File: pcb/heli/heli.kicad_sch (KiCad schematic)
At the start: 33 parts, among them J1 Batterie, J2 Debug, J4 Servo, J5 Servo, Q1 IRLZ44N, SW1 SW_MEC_5E, U1 AZ1117-3.3, U2 MPU-6050, U3 STM32F103CBTx, Y1 8MHz

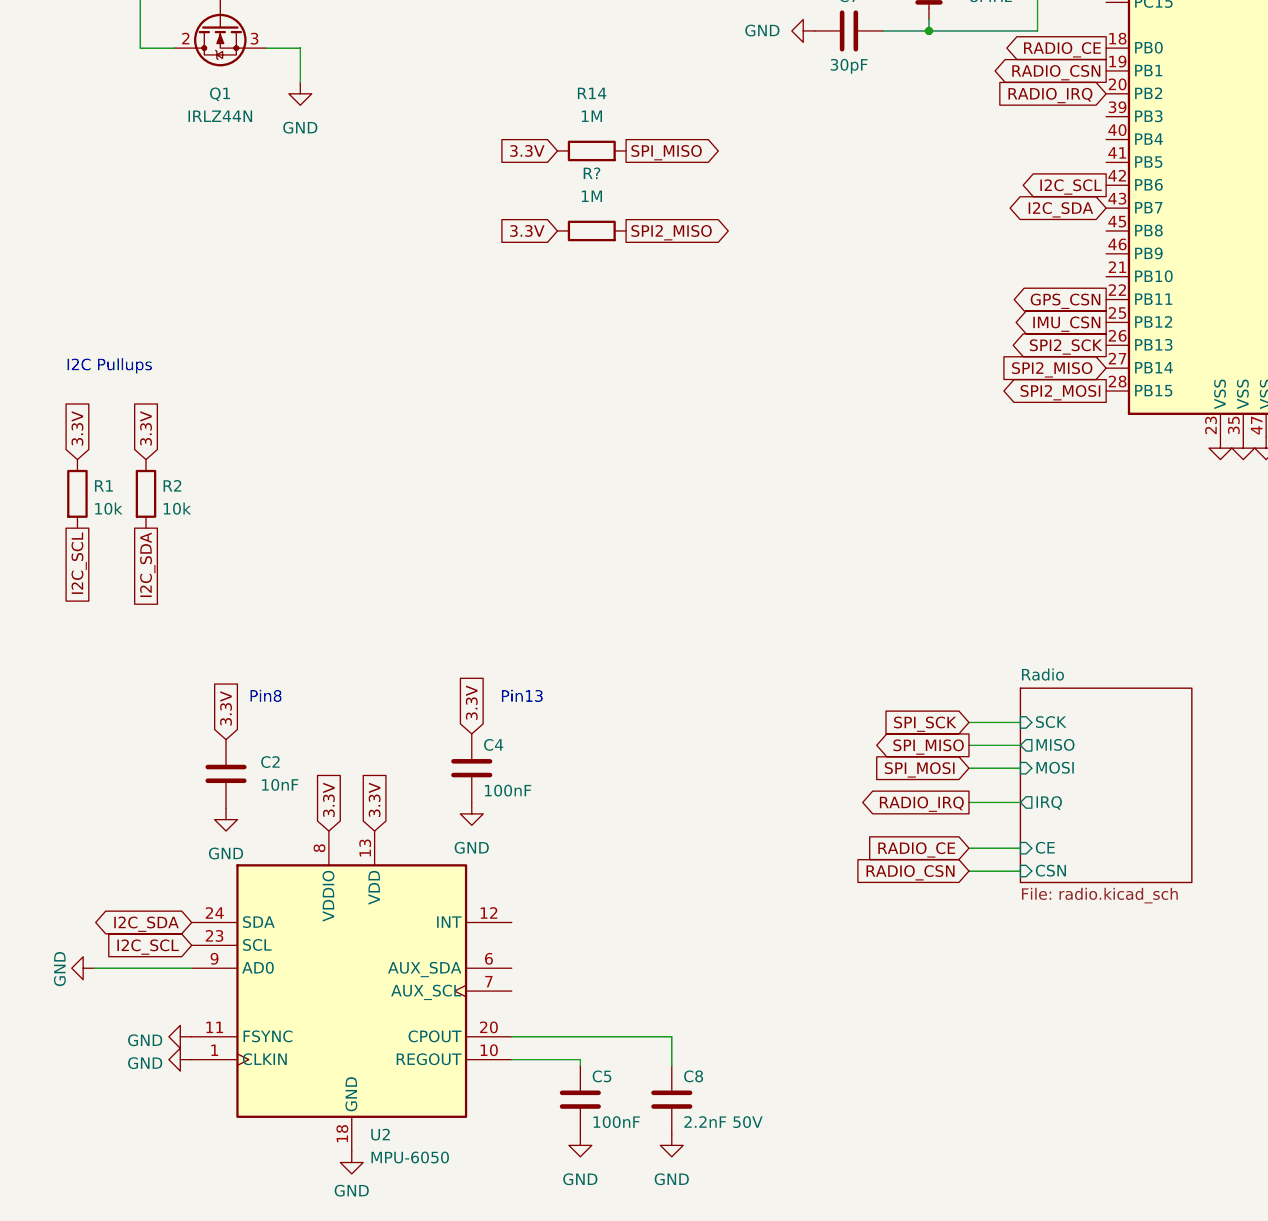
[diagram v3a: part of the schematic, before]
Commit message: Removed MPU6050, updated pcb
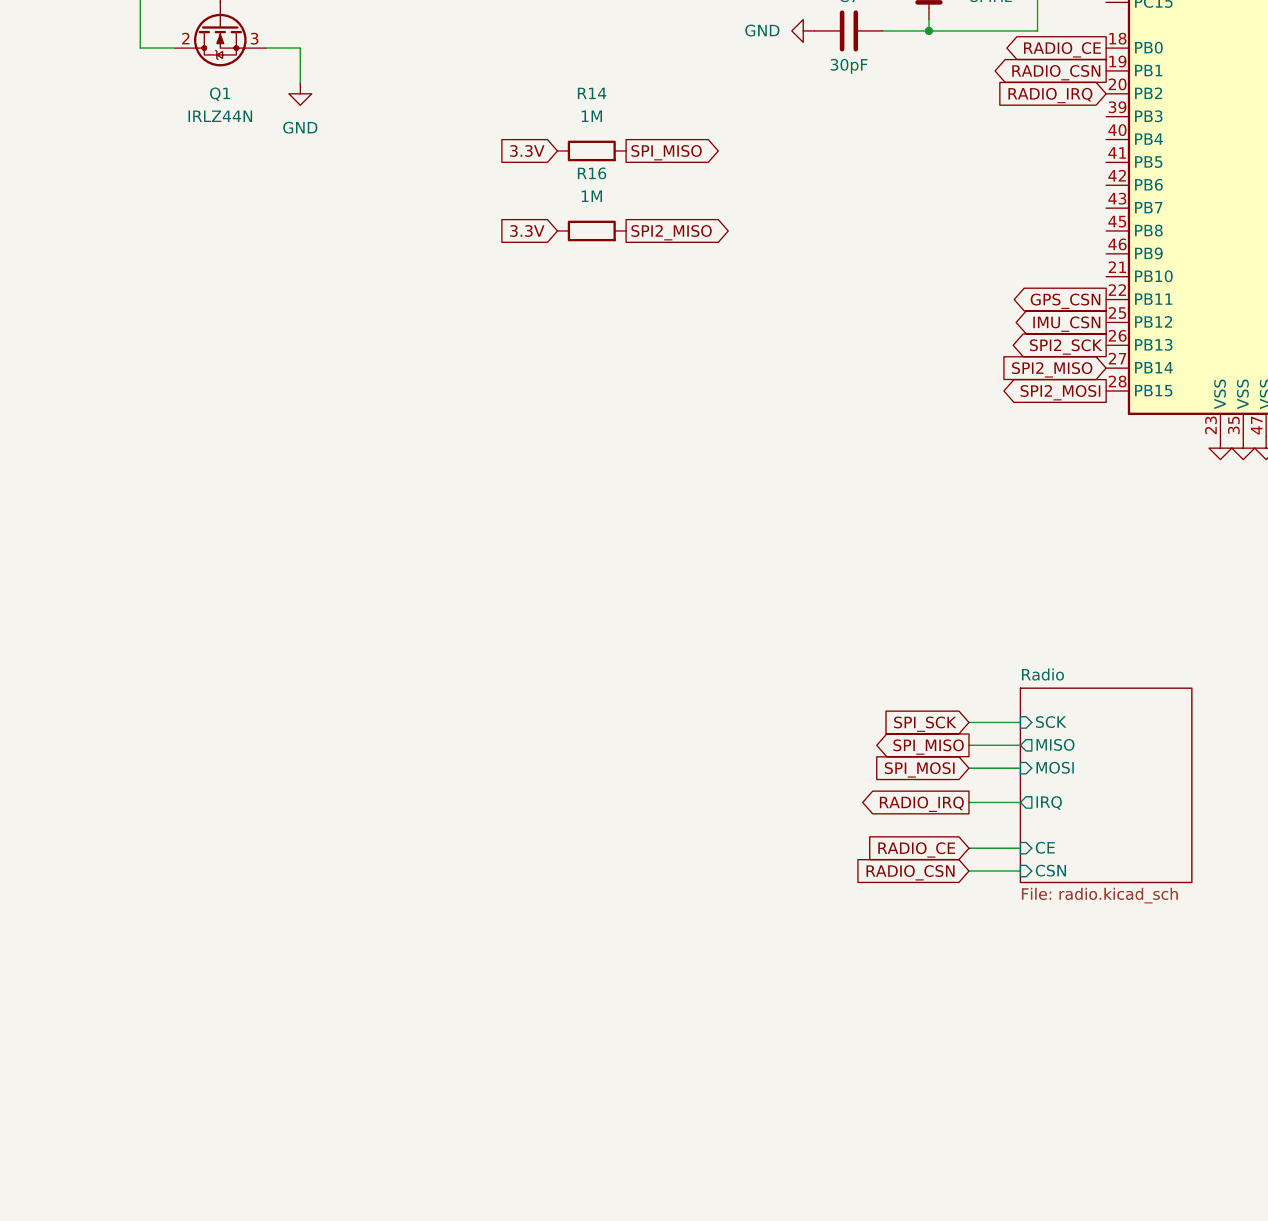
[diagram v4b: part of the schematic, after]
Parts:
- removed C2: 10nF, Capacitor_SMD:C_0603_1608Metric, symbol Device:C
- removed C4, C5: 100nF, Capacitor_SMD:C_0603_1608Metric, symbol Device:C
- removed C8: 2.2nF 50V, Capacitor_SMD:C_0603_1608Metric, symbol Device:C
- removed R1, R2: 10k, Resistor_SMD:R_0603_1608Metric, symbol Device:R
- removed U2: MPU-6050, Sensor_Motion:InvenSense_QFN-24_4x4mm_P0.5mm, symbol Sensor_Motion:MPU-6050
- gave numbers to parts that had none: 1
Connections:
- net I2C_SCL: no longer names the net of U3.42 (PB6)
- net I2C_SDA: no longer names the net of U3.43 (PB7)
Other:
- note removed: "I2C Pullups"
- note removed: "Pin13"
- note removed: "Pin8"

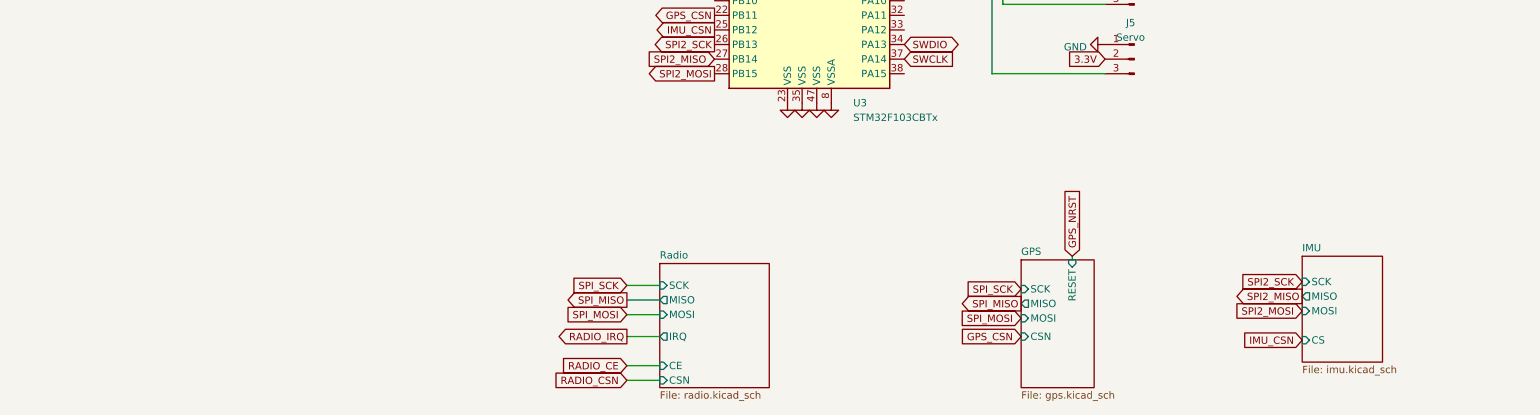
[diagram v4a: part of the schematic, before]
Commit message: Added BMM150 as BMI270 i2c slave
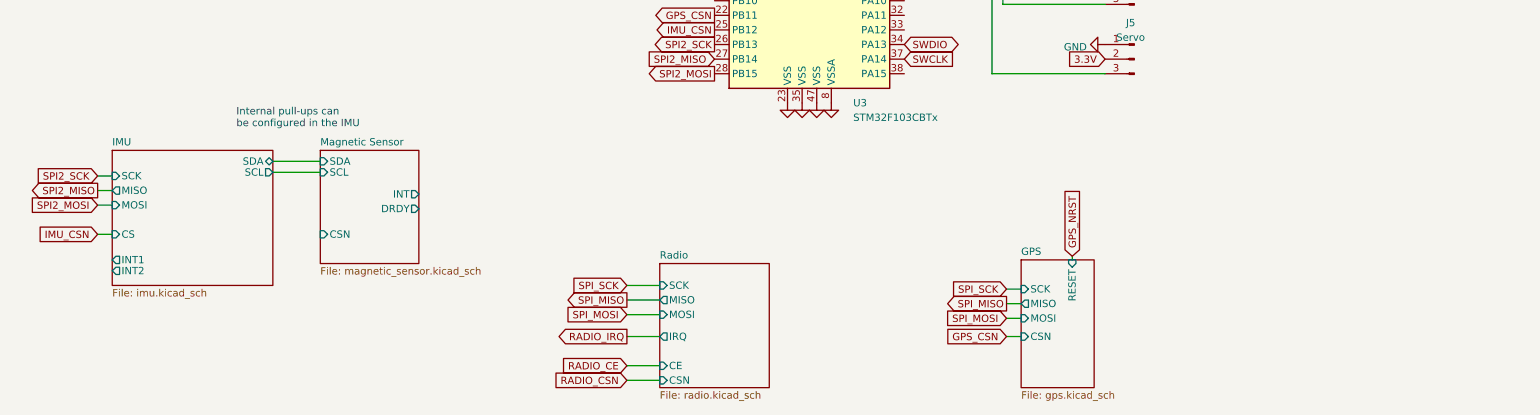
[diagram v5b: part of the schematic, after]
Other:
- added sheet Magnetic Sensor (magnetic_sensor.kicad_sch)
- sheet IMU ports: added INT1, INT2, SCL, SDA; removed none
- note added: "Internal pull-ups can be configured in the IMU"

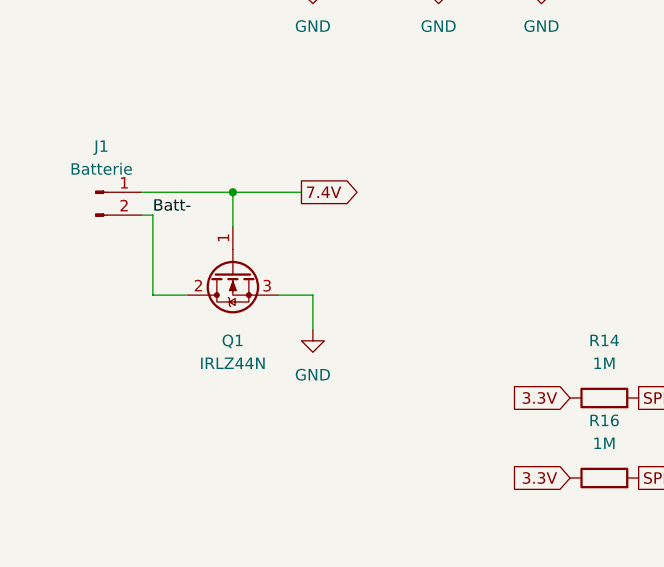
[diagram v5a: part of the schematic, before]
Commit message: 
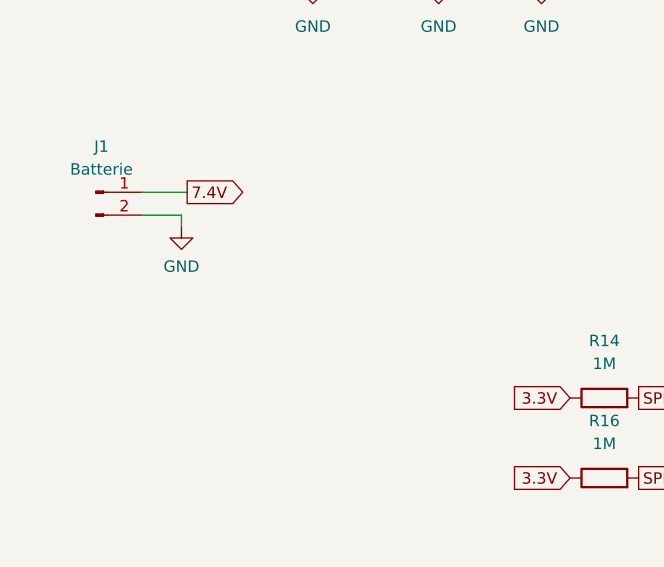
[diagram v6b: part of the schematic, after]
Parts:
- removed Q1: IRLZ44N, Package_TO_SOT_THT:TO-220-3_Vertical, symbol Transistor_FET:IRLZ44N
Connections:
- net Batt- is gone; now on net GND: J1.2 (Pin_2)
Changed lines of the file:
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@@
   (junction (at 271.78 32.385) (diameter 0) (color 0 0 0 0)
   )
-  (junction (at 38.1 55.88) (diameter 0) (color 0 0 0 0)
-  )
   (junction (at 156.845 31.75) (diameter 0) (color 0 0 0 0)
   )
@@
     (stroke (width 0) (type default) (color 0 0 0 0))
   )
+  (wire (pts (xy 32.385 59.69) (xy 32.385 58.42))
+    (stroke (width 0) (type default) (color 0 0 0 0))
+  )
   (wire (pts (xy 207.645 31.115) (xy 207.645 32.385))
     (stroke (width 0) (type default) (color 0 0 0 0))
@@
     (stroke (width 0) (type default) (color 0 0 0 0))
   )
-  (wire (pts (xy 38.1 55.88) (xy 38.1 59.69))
-    (stroke (width 0) (type default) (color 0 0 0 0))
-  )
   (wire (pts (xy 184.785 74.93) (xy 184.785 105.41))
     (stroke (width 0) (type default) (color 0 0 0 0))
   )
-  (wire (pts (xy 38.1 55.88) (xy 45.72 55.88))
-    (stroke (width 0) (type default) (color 0 0 0 0))
-  )
   (wire (pts (xy 125.095 44.45) (xy 136.525 44.45))
     (stroke (width 0) (type default) (color 0 0 0 0))
@@
     (stroke (width 0) (type default) (color 0 0 0 0))
   )
-  (wire (pts (xy 46.99 67.31) (xy 46.99 71.12))
-    (stroke (width 0) (type default) (color 0 0 0 0))
-  )
-  (wire (pts (xy 27.94 55.88) (xy 38.1 55.88))
+  (wire (pts (xy 27.94 55.88) (xy 33.02 55.88))
     (stroke (width 0) (type default) (color 0 0 0 0))
   )
@@
     (stroke (width 0) (type default) (color 0 0 0 0))
   )
-  (wire (pts (xy 29.21 58.42) (xy 29.21 67.31))
-    (stroke (width 0) (type default) (color 0 0 0 0))
-  )
   (wire (pts (xy 59.69 122.555) (xy 67.945 122.555))
     (stroke (width 0) (type default) (color 0 0 0 0))
@@
     (stroke (width 0) (type default) (color 0 0 0 0))
   )
+  (wire (pts (xy 32.385 58.42) (xy 27.94 58.42))
+    (stroke (width 0) (type default) (color 0 0 0 0))
+  )
   (wire (pts (xy 271.78 37.465) (xy 271.78 32.385))
     (stroke (width 0) (type default) (color 0 0 0 0))
@@
     (stroke (width 0) (type default) (color 0 0 0 0))
   )
-  (wire (pts (xy 33.02 67.31) (xy 29.21 67.31))
-    (stroke (width 0) (type default) (color 0 0 0 0))
-  )
   (wire (pts (xy 184.785 105.41) (xy 204.47 105.41))
-    (stroke (width 0) (type default) (color 0 0 0 0))
-  )
-  (wire (pts (xy 27.94 58.42) (xy 29.21 58.42))
-    (stroke (width 0) (type default) (color 0 0 0 0))
-  )
-  (wire (pts (xy 43.18 67.31) (xy 46.99 67.31))
     (stroke (width 0) (type default) (color 0 0 0 0))
   )
@@
   )
   (label "PWM2" (at 174.625 69.85 0)
-    (effects (font (size 1.27 1.27)) (justify left bottom))
-  )
-  (label "Batt-" (at 29.21 58.42 0)
     (effects (font (size 1.27 1.27)) (justify left bottom))
   )
@@
     )
   )
-  (global_label "7.4V" (shape output) (at 45.72 55.88 0) (fields_autoplaced)
+  (global_label "7.4V" (shape output) (at 33.02 55.88 0) (fields_autoplaced)
     (effects (font (size 1.27 1.27)) (justify left))
-    (property "Intersheet References" "${INTERSHEET_REFS}" (id 0) (at 52.2455 55.8006 0)
+    (property "Intersheet References" "${INTERSHEET_REFS}" (id 0) (at 39.5455 55.8006 0)
       (effects (font (size 1.27 1.27)) (justify left) hide)
     )
@@
     )
     (pin "1")
-  )
-  (symbol (lib_id "Transistor_FET:IRLZ44N") (at 38.1 64.77 90) (mirror x) (unit 1)
-    (in_bom yes) (on_board yes) (fields_autoplaced)
-    (property "Reference" "Q1" (id 0) (at 38.1 72.39 90))
-    (property "Value" "IRLZ44N" (id 1) (at 38.1 74.93 90))
-    (property "Footprint" "Package_TO_SOT_THT:TO-220-3_Vertical" (id 2) (at 40.005 71.12 0)
-      (effects (font (size 1.27 1.27) italic) (justify left) hide)
-    )
-    (property "Datasheet" "http://www.irf.com/product-info/datasheets/data/irlz44n.pdf" (id 3) (at 38.1 64.77 0)
-      (effects (font (size 1.27 1.27)) (justify left) hide)
-    )
-    (property "DIGIKEY" "-" (id 4) (at 38.1 64.77 0)
-      (effects (font (size 1.27 1.27)) hide)
-    )
-    (pin "1")
-    (pin "2")
-    (pin "3")
   )
   (symbol (lib_id "Device:R") (at 79.375 78.74 90) (unit 1)
@@
     (pin "2")
   )
-  (symbol (lib_id "power:GND") (at 46.99 71.12 0) (unit 1)
-    (in_bom yes) (on_board yes) (fields_autoplaced)
-    (property "Reference" "#PWR02" (id 0) (at 46.99 77.47 0)
-      (effects (font (size 1.27 1.27)) hide)
-    )
-    (property "Value" "GND" (id 1) (at 46.99 76.2 0))
-    (property "Footprint" "" (id 2) (at 46.99 71.12 0)
-      (effects (font (size 1.27 1.27)) hide)
-    )
-    (property "Datasheet" "" (id 3) (at 46.99 71.12 0)
+  (symbol (lib_id "power:GND") (at 32.385 59.69 0) (unit 1)
+    (in_bom yes) (on_board yes) (fields_autoplaced)
+    (property "Reference" "#PWR02" (id 0) (at 32.385 66.04 0)
+      (effects (font (size 1.27 1.27)) hide)
+    )
+    (property "Value" "GND" (id 1) (at 32.385 64.135 0))
+    (property "Footprint" "" (id 2) (at 32.385 59.69 0)
+      (effects (font (size 1.27 1.27)) hide)
+    )
+    (property "Datasheet" "" (id 3) (at 32.385 59.69 0)
       (effects (font (size 1.27 1.27)) hide)
     )
@@
       (reference "M2") (unit 1) (value "Motor_DC") (footprint "Connector_PinHeader_2.54mm:PinHeader_1x02_P2.54mm_Vertical")
     )
-    (path "/1bc1b3d0-4ecf-47f2-9895-078f1ce0371b"
-      (reference "Q1") (unit 1) (value "IRLZ44N") (footprint "Package_TO_SOT_THT:TO-220-3_Vertical")
-    )
     (path "/c5583cdf-ca59-48f7-a91f-20c1806ad1c1/4cdb332b-134c-43a6-bf7e-ba3ca71c9153"

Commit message: 
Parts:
- C14: footprint Capacitor_SMD:CP_Elec_5x5.4 -> Capacitor_SMD:C_0603_1608Metric; DIGIKEY - -> 1276-1119-1-ND
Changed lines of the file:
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@@
       (effects (font (size 1.27 1.27)) (justify left))
     )
-    (property "Footprint" "Capacitor_SMD:CP_Elec_5x5.4" (id 2) (at 228.2952 31.115 0)
+    (property "Footprint" "Capacitor_SMD:C_0603_1608Metric" (id 2) (at 228.2952 31.115 0)
       (effects (font (size 1.27 1.27)) hide)
     )
@@
       (effects (font (size 1.27 1.27)) hide)
     )
-    (property "DIGIKEY" "-" (id 4) (at 227.33 27.305 0)
+    (property "DIGIKEY" "1276-1119-1-ND" (id 4) (at 227.33 27.305 0)
       (effects (font (size 1.27 1.27)) hide)
     )
@@
     )
     (path "/aa122ab8-03e5-4c5e-a007-ec3e3f5864b8"
-      (reference "C14") (unit 1) (value "10uF") (footprint "Capacitor_SMD:CP_Elec_5x5.4")
+      (reference "C14") (unit 1) (value "10uF") (footprint "Capacitor_SMD:C_0603_1608Metric")
     )
     (path "/431ea231-a812-4481-addf-46e53a5f0cb7"
@@
     )
     (path "/ff163e09-1c9a-4e9f-9fc2-cd2f8ec1c6f1/2fd26247-c389-46da-87ab-ae44b6585d62"
-      (reference "C28") (unit 1) (value "1uF") (footprint "Capacitor_SMD:CP_Elec_4x5.4")
+      (reference "C28") (unit 1) (value "10uF") (footprint "Capacitor_SMD:C_0603_1608Metric")
     )
     (path "/8972c389-56a6-466a-9271-66b0ec918c0e/05f17882-cc20-49a8-a23e-123bfd3a173c"

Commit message: Manufacturing Candidate
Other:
- sheet Magnetic Sensor ports: added none; removed CSN
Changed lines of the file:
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@@
       (effects (font (size 1.27 1.27)) (justify right))
-    )
-    (pin "CSN" input (at 67.945 133.35 180)
-      (effects (font (size 1.27 1.27)) (justify left))
     )
     (pin "SDA" input (at 67.945 120.65 180)
